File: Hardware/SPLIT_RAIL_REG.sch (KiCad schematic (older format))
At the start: 21 parts, among them Q1 PMOS, U1 TPS65130

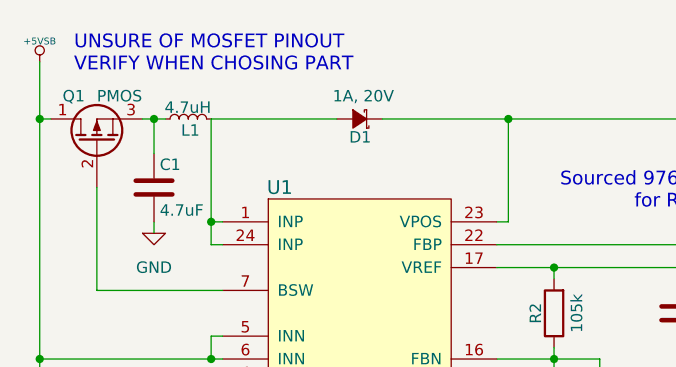
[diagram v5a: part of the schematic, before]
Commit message: Fixed schematic errors, added muse-v2-lib
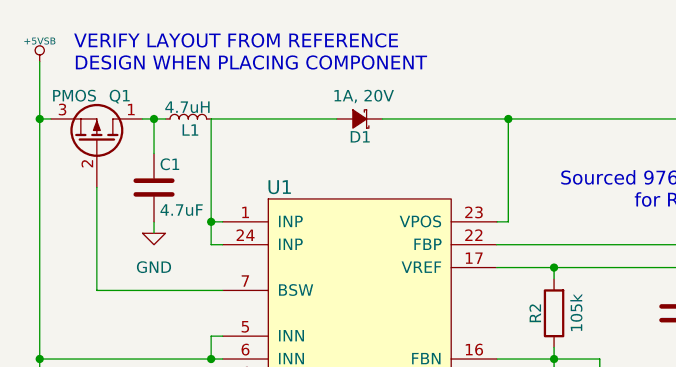
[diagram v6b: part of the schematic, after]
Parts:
- C1, C4, C5, C6, C7, C8, C9: footprint (none) -> Capacitors_SMD:C_0603
- C10, C3: footprint (none) -> Capacitors_SMD:C_1206
- C2: footprint (none) -> Capacitors_SMD:C_0402
- L1, L2: footprint (none) -> Choke_SMD:Choke_SMD_7.3x7.3_H3.5
- Q1: footprint (none) -> TO_SOT_Packages_SMD:SOT-23
- R1, R2, R3, R4, R5: footprint (none) -> Resistors_SMD:R_0402
- U1: footprint (none) -> MF_Switches:MF_Switches-TACT4.2MM
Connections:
- net +5VSB: now also Q1.3 (S); no longer Q1.1 (D)
- net at C1.1, L1.1: now also Q1.1 (D); no longer Q1.3 (S)
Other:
- note added: "VERIFY LAYOUT FROM REFERENCE\nDESIGN WHEN PLACING COMPONENT"
- note removed: "UNSURE OF MOSFET PINOUT\nVERIFY WHEN CHOSING PART"
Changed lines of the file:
@@
 F 0 "U1" H 5100 2950 60  0000 C CNN
 F 1 "TPS65130" H 5800 1150 60  0000 C CNN
-F 2 "" H 5050 2900 60  0001 C CNN
+F 2 "MF_Switches:MF_Switches-TACT4.2MM" H 5050 2900 60  0001 C CNN
 F 3 "" H 5050 2900 60  0001 C CNN
 	1    5050 2900
@@
 $EndComp
 $Comp
-L GND-RESCUE-museV2-RESCUE-museV2 #PWR01
+L GND-RESCUE-museV2-RESCUE-museV2 #PWR10
 U 1 1 57DAC9F2
 P 5450 5000
-F 0 "#PWR01" H 5450 4750 50  0001 C CNN
+F 0 "#PWR10" H 5450 4750 50  0001 C CNN
 F 1 "GND" H 5450 4850 50  0000 C CNN
 F 2 "" H 5450 5000 50  0000 C CNN
@@
 F 0 "C8" H 6125 4850 50  0000 L CNN
 F 1 "10nF" H 6125 4650 50  0000 L CNN
-F 2 "" H 6138 4600 50  0000 C CNN
+F 2 "Capacitors_SMD:C_0603" H 6138 4600 50  0001 C CNN
 F 3 "10 nF, ceramic, 16 V, X7R" H 6100 4750 50  0001 C CNN
 	1    6100 4750
@@
 F 0 "C9" H 6375 4850 50  0000 L CNN
 F 1 "4.7nF" H 6375 4650 50  0000 L CNN
-F 2 "" H 6388 4600 50  0000 C CNN
+F 2 "Capacitors_SMD:C_0603" H 6388 4600 50  0001 C CNN
 F 3 "4.7 nF, 50 V, C0G" H 6350 4750 50  0001 C CNN
 	1    6350 4750
@@
 $EndComp
 $Comp
-L GND-RESCUE-museV2-RESCUE-museV2 #PWR02
+L GND-RESCUE-museV2-RESCUE-museV2 #PWR11
 U 1 1 57DACA83
 P 6100 5000
-F 0 "#PWR02" H 6100 4750 50  0001 C CNN
+F 0 "#PWR11" H 6100 4750 50  0001 C CNN
 F 1 "GND" H 6100 4850 50  0000 C CNN
 F 2 "" H 6100 5000 50  0000 C CNN
@@
 $EndComp
 $Comp
-L GND-RESCUE-museV2-RESCUE-museV2 #PWR03
+L GND-RESCUE-museV2-RESCUE-museV2 #PWR12
 U 1 1 57DACA97
 P 6350 5000
-F 0 "#PWR03" H 6350 4750 50  0001 C CNN
+F 0 "#PWR12" H 6350 4750 50  0001 C CNN
 F 1 "GND" H 6350 4850 50  0000 C CNN
 F 2 "" H 6350 5000 50  0000 C CNN
@@
 F 0 "L2" H 6630 4790 50  0000 L CNN
 F 1 "4.7uH" H 6630 4710 50  0000 L CNN
-F 2 "" H 6600 4750 50  0000 C CNN
+F 2 "Choke_SMD:Choke_SMD_7.3x7.3_H3.5" H 6600 4750 50  0001 C CNN
 F 3 "Wurth Elektronik 7447789004" H 6600 4750 50  0001 C CNN
 	1    6600 4750
@@
 $EndComp
 $Comp
-L GND-RESCUE-museV2-RESCUE-museV2 #PWR04
+L GND-RESCUE-museV2-RESCUE-museV2 #PWR13
 U 1 1 57DACC08
 P 6600 5000
-F 0 "#PWR04" H 6600 4750 50  0001 C CNN
+F 0 "#PWR13" H 6600 4750 50  0001 C CNN
 F 1 "GND" H 6600 4850 50  0000 C CNN
 F 2 "" H 6600 5000 50  0000 C CNN
@@
 $EndComp
 $Comp
-L GND-RESCUE-museV2-RESCUE-museV2 #PWR05
+L GND-RESCUE-museV2-RESCUE-museV2 #PWR14
 U 1 1 57DACD4E
 P 7550 5000
-F 0 "#PWR05" H 7550 4750 50  0001 C CNN
+F 0 "#PWR14" H 7550 4750 50  0001 C CNN
 F 1 "GND" H 7550 4850 50  0000 C CNN
 F 2 "" H 7550 5000 50  0000 C CNN
@@
 F 0 "R4" V 6200 3800 50  0000 C CNN
 F 1 "1.3M" V 6300 3800 50  0000 C CNN
-F 2 "" V 6230 3800 50  0000 C CNN
+F 2 "Resistors_SMD:R_0402" V 6230 3800 50  0001 C CNN
 F 3 "" H 6300 3800 50  0000 C CNN
 	1    6300 3800
@@
 F 0 "C5" H 6525 3900 50  0000 L CNN
 F 1 "5.77pF" H 6525 3700 50  0000 L CNN
-F 2 "" H 6538 3650 50  0000 C CNN
+F 2 "Capacitors_SMD:C_0603" H 6538 3650 50  0001 C CNN
 F 3 "" H 6500 3800 50  0000 C CNN
 	1    6500 3800
@@
 F 0 "R2" V 6380 3400 50  0000 C CNN
 F 1 "105k" V 6200 3400 50  0000 C CNN
-F 2 "" V 6230 3400 50  0000 C CNN
+F 2 "Resistors_SMD:R_0402" V 6230 3400 50  0001 C CNN
 F 3 "" H 6300 3400 50  0000 C CNN
 	1    6300 3400
@@
 F 0 "C4" H 6875 3500 50  0000 L CNN
 F 1 "220nF" H 6875 3300 50  0000 L CNN
-F 2 "" H 6888 3250 50  0000 C CNN
+F 2 "Capacitors_SMD:C_0603" H 6888 3250 50  0001 C CNN
 F 3 "220 nF, ceramic, 6.3 V, X5R" H 6850 3400 50  0001 C CNN
 	1    6850 3400
@@
 Connection ~ 6300 3200
 $Comp
-L GND-RESCUE-museV2-RESCUE-museV2 #PWR06
+L GND-RESCUE-museV2-RESCUE-museV2 #PWR4
 U 1 1 57DADA89
 P 6850 3750
-F 0 "#PWR06" H 6850 3500 50  0001 C CNN
+F 0 "#PWR4" H 6850 3500 50  0001 C CNN
 F 1 "GND" H 6850 3600 50  0000 C CNN
 F 2 "" H 6850 3750 50  0000 C CNN
@@
 F 0 "C7" H 4575 4850 50  0000 L CNN
 F 1 "100nF" H 4575 4650 50  0000 L CNN
-F 2 "" H 4588 4600 50  0000 C CNN
+F 2 "Capacitors_SMD:C_0603" H 4588 4600 50  0001 C CNN
 F 3 "0.1 µF, ceramic, 10 V, X5R" H 4550 4750 50  0001 C CNN
 	1    4550 4750
@@
 F 0 "R5" V 4380 4500 50  0000 C CNN
 F 1 "100" V 4300 4500 50  0000 C CNN
-F 2 "" V 4230 4500 50  0000 C CNN
+F 2 "Resistors_SMD:R_0402" V 4230 4500 50  0001 C CNN
 F 3 "" H 4300 4500 50  0000 C CNN
 	1    4300 4500
@@
 	4050 4500 4150 4500
 $Comp
-L GND-RESCUE-museV2-RESCUE-museV2 #PWR07
+L GND-RESCUE-museV2-RESCUE-museV2 #PWR9
 U 1 1 57DAE30A
 P 4550 5000
-F 0 "#PWR07" H 4550 4750 50  0001 C CNN
+F 0 "#PWR9" H 4550 4750 50  0001 C CNN
 F 1 "GND" H 4550 4850 50  0000 C CNN
 F 2 "" H 4550 5000 50  0000 C CNN
@@
 	4550 5000 4550 4900
 $Comp
-L GND-RESCUE-museV2-RESCUE-museV2 #PWR08
+L GND-RESCUE-museV2-RESCUE-museV2 #PWR8
 U 1 1 57DAE3B0
 P 4050 5000
-F 0 "#PWR08" H 4050 4750 50  0001 C CNN
+F 0 "#PWR8" H 4050 4750 50  0001 C CNN
 F 1 "GND" H 4050 4850 50  0000 C CNN
 F 2 "" H 4050 5000 50  0000 C CNN
@@
 F 0 "Q1" V 4500 2800 50  0000 R CNN
 F 1 "PMOS" V 4500 2650 50  0000 R CNN
-F 2 "" H 4500 2750 50  0000 C CNN
+F 2 "TO_SOT_Packages_SMD:SOT-23" H 4500 2750 50  0001 C CNN
 F 3 "MOSFET, P-channel, 12 V, 4 A, Vishay" H 4300 2650 50  0001 C CNN
 	1    4300 2650
-	0    -1   -1   0
+	0    1    -1   0
 $EndComp
 Connection ~ 4050 2550
@@
 F 0 "C1" H 4575 2950 50  0000 L CNN
 F 1 "4.7uF" H 4575 2750 50  0000 L CNN
-F 2 "" H 4588 2700 50  0000 C CNN
+F 2 "Capacitors_SMD:C_0603" H 4588 2700 50  0001 C CNN
 F 3 "4.7 µF, ceramic, 6.3 V, X5R" H 4550 2850 50  0001 C CNN
 	1    4550 2850
@@
 $EndComp
 $Comp
-L GND-RESCUE-museV2-RESCUE-museV2 #PWR09
+L GND-RESCUE-museV2-RESCUE-museV2 #PWR3
 U 1 1 57DAEBCD
 P 4550 3050
-F 0 "#PWR09" H 4550 2800 50  0001 C CNN
+F 0 "#PWR3" H 4550 2800 50  0001 C CNN
 F 1 "GND" H 4550 2900 50  0000 C CNN
 F 2 "" H 4550 3050 50  0000 C CNN
@@
 F 0 "D1" H 5400 2630 50  0000 L CNN
 F 1 "1A, 20V" H 5300 2450 50  0000 L CNN
-F 2 "" V 5450 2550 50  0000 C CNN
+F 2 "" V 5450 2550 50  0001 C CNN
 F 3 "Schottky, 1 A, 20 V, Onsemi MBRM120" V 5450 2550 50  0001 C CNN
 	1    5450 2550
@@
 F 0 "R3" V 7330 3400 50  0000 C CNN
 F 1 "85.8k" V 7150 3400 50  0000 C CNN
-F 2 "" V 7180 3400 50  0000 C CNN
+F 2 "Resistors_SMD:R_0402" V 7180 3400 50  0001 C CNN
 F 3 "" H 7250 3400 50  0000 C CNN
 	1    7250 3400
@@
 $EndComp
 $Comp
-L GND-RESCUE-museV2-RESCUE-museV2 #PWR010
+L GND-RESCUE-museV2-RESCUE-museV2 #PWR5
 U 1 1 57DAF32E
 P 7250 3750
-F 0 "#PWR010" H 7250 3500 50  0001 C CNN
+F 0 "#PWR5" H 7250 3500 50  0001 C CNN
 F 1 "GND" H 7250 3600 50  0000 C CNN
 F 2 "" H 7250 3750 50  0000 C CNN
@@
 F 0 "R1" V 7130 2850 50  0000 C CNN
 F 1 "975k" V 7050 2850 50  0000 C CNN
-F 2 "" V 6980 2850 50  0000 C CNN
+F 2 "Resistors_SMD:R_0402" V 6980 2850 50  0001 C CNN
 F 3 "" H 7050 2850 50  0000 C CNN
 	1    7050 2850
@@
 F 0 "C2" H 7275 2950 50  0000 L CNN
 F 1 "6.97pF" H 7275 2750 50  0000 L CNN
-F 2 "" H 7288 2700 50  0000 C CNN
+F 2 "Capacitors_SMD:C_0402" H 7288 2700 50  0001 C CNN
 F 3 "" H 7250 2850 50  0000 C CNN
 	1    7250 2850
@@
 F 0 "C3" H 7575 2950 50  0000 L CNN
 F 1 "4.7uF" H 7575 2750 50  0000 L CNN
-F 2 "" H 7588 2700 50  0000 C CNN
+F 2 "Capacitors_SMD:C_1206" H 7588 2700 50  0001 C CNN
 F 3 "4 x 4.7 µF, ceramic, 25 V, X7R" H 7550 2850 50  0001 C CNN
 	1    7550 2850
@@
 Connection ~ 7550 2550
 $Comp
-L GND-RESCUE-museV2-RESCUE-museV2 #PWR011
+L GND-RESCUE-museV2-RESCUE-museV2 #PWR6
 U 1 1 57DAF96B
 P 7550 3750
-F 0 "#PWR011" H 7550 3500 50  0001 C CNN
+F 0 "#PWR6" H 7550 3500 50  0001 C CNN
 F 1 "GND" H 7550 3600 50  0000 C CNN
 F 2 "" H 7550 3750 50  0000 C CNN
@@
 F 0 "C6" H 4075 4850 50  0000 L CNN
 F 1 "4.7uF" H 4075 4650 50  0000 L CNN
-F 2 "" H 4088 4600 50  0000 C CNN
+F 2 "Capacitors_SMD:C_0603" H 4088 4600 50  0001 C CNN
 F 3 "4.7 µF, ceramic, 6.3 V, X5R" H 4050 4750 50  0001 C CNN
 	1    4050 4750
@@
 F 0 "C10" H 7575 4850 50  0000 L CNN
 F 1 "4.7uF" H 7575 4650 50  0000 L CNN
-F 2 "" H 7588 4600 50  0000 C CNN
+F 2 "Capacitors_SMD:C_1206" H 7588 4600 50  0001 C CNN
 F 3 "4 x 4.7 µF, ceramic, 25 V, X7R" H 7550 4750 50  0001 C CNN
 	1    7550 4750
@@
 F 0 "L1" V 4650 2500 50  0000 L CNN
 F 1 "4.7uH" V 4750 2450 50  0000 L CNN
-F 2 "" H 4700 2550 50  0000 C CNN
+F 2 "Choke_SMD:Choke_SMD_7.3x7.3_H3.5" H 4700 2550 50  0001 C CNN
 F 3 "Wurth Elektronik 7447789004" H 4700 2550 50  0001 C CNN
 	1    4700 2550
@@
 $EndComp
 Text Notes 4200 2350 0    60   ~ 0
-UNSURE OF MOSFET PINOUT\nVERIFY WHEN CHOSING PART
+VERIFY LAYOUT FROM REFERENCE\nDESIGN WHEN PLACING COMPONENT
 $Comp
 L D_Schottky_Small D2
@@
 F 0 "D2" H 7000 4280 50  0000 L CNN
 F 1 "1A, 20V" H 6900 4100 50  0000 L CNN
-F 2 "" V 7050 4200 50  0000 C CNN
+F 2 "" V 7050 4200 50  0001 C CNN
 F 3 "Schottky, 1 A, 20 V, Onsemi MBRM120" V 7050 4200 50  0001 C CNN
 	1    7050 4200
@@
 $EndComp
 $Comp
-L +5VSB #PWR012
+L +5VSB #PWR1
 U 1 1 57F87DFC
 P 4050 2300
-F 0 "#PWR012" H 4050 2390 20  0001 C CNN
+F 0 "#PWR1" H 4050 2390 20  0001 C CNN
 F 1 "+5VSB" H 4050 2390 30  0000 C CNN
 F 2 "" H 4050 2300 60  0000 C CNN
@@
 	7850 2550 7850 2300
 $Comp
-L +15VSB #PWR013
+L +15VSB #PWR2
 U 1 1 57F88166
 P 7850 2300
-F 0 "#PWR013" H 7850 2150 50  0001 C CNN
+F 0 "#PWR2" H 7850 2150 50  0001 C CNN
 F 1 "+15VSB" H 7850 2440 50  0000 C CNN
 F 2 "" H 7850 2300 50  0000 C CNN

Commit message: Added proper audio connectors to schematic
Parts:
- D1, D2: footprint (none) -> muse-v2-lib:DO-216-AA
- L1, L2: footprint Choke_SMD:Choke_SMD_7.3x7.3_H3.5 -> muse-v2-lib:7.3mm-Inductor
- U1: footprint MF_Switches:MF_Switches-TACT4.2MM -> Housings_DFN_QFN:QFN-24-1EP_4x4mm_Pitch0.5mm
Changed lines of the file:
@@
 F 0 "U1" H 5100 2950 60  0000 C CNN
 F 1 "TPS65130" H 5800 1150 60  0000 C CNN
-F 2 "MF_Switches:MF_Switches-TACT4.2MM" H 5050 2900 60  0001 C CNN
+F 2 "Housings_DFN_QFN:QFN-24-1EP_4x4mm_Pitch0.5mm" H 5050 2900 60  0001 C CNN
 F 3 "" H 5050 2900 60  0001 C CNN
 	1    5050 2900
@@
 $EndComp
 $Comp
-L GND-RESCUE-museV2-RESCUE-museV2 #PWR10
+L GND-RESCUE-museV2-RESCUE-museV2 #PWR01
 U 1 1 57DAC9F2
 P 5450 5000
-F 0 "#PWR10" H 5450 4750 50  0001 C CNN
+F 0 "#PWR01" H 5450 4750 50  0001 C CNN
 F 1 "GND" H 5450 4850 50  0000 C CNN
 F 2 "" H 5450 5000 50  0000 C CNN
@@
 $EndComp
 $Comp
-L GND-RESCUE-museV2-RESCUE-museV2 #PWR11
+L GND-RESCUE-museV2-RESCUE-museV2 #PWR02
 U 1 1 57DACA83
 P 6100 5000
-F 0 "#PWR11" H 6100 4750 50  0001 C CNN
+F 0 "#PWR02" H 6100 4750 50  0001 C CNN
 F 1 "GND" H 6100 4850 50  0000 C CNN
 F 2 "" H 6100 5000 50  0000 C CNN
@@
 $EndComp
 $Comp
-L GND-RESCUE-museV2-RESCUE-museV2 #PWR12
+L GND-RESCUE-museV2-RESCUE-museV2 #PWR03
 U 1 1 57DACA97
 P 6350 5000
-F 0 "#PWR12" H 6350 4750 50  0001 C CNN
+F 0 "#PWR03" H 6350 4750 50  0001 C CNN
 F 1 "GND" H 6350 4850 50  0000 C CNN
 F 2 "" H 6350 5000 50  0000 C CNN
@@
 F 0 "L2" H 6630 4790 50  0000 L CNN
 F 1 "4.7uH" H 6630 4710 50  0000 L CNN
-F 2 "Choke_SMD:Choke_SMD_7.3x7.3_H3.5" H 6600 4750 50  0001 C CNN
+F 2 "muse-v2-lib:7.3mm-Inductor" H 6600 4750 50  0001 C CNN
 F 3 "Wurth Elektronik 7447789004" H 6600 4750 50  0001 C CNN
 	1    6600 4750
@@
 $EndComp
 $Comp
-L GND-RESCUE-museV2-RESCUE-museV2 #PWR13
+L GND-RESCUE-museV2-RESCUE-museV2 #PWR04
 U 1 1 57DACC08
 P 6600 5000
-F 0 "#PWR13" H 6600 4750 50  0001 C CNN
+F 0 "#PWR04" H 6600 4750 50  0001 C CNN
 F 1 "GND" H 6600 4850 50  0000 C CNN
 F 2 "" H 6600 5000 50  0000 C CNN
@@
 $EndComp
 $Comp
-L GND-RESCUE-museV2-RESCUE-museV2 #PWR14
+L GND-RESCUE-museV2-RESCUE-museV2 #PWR05
 U 1 1 57DACD4E
 P 7550 5000
-F 0 "#PWR14" H 7550 4750 50  0001 C CNN
+F 0 "#PWR05" H 7550 4750 50  0001 C CNN
 F 1 "GND" H 7550 4850 50  0000 C CNN
 F 2 "" H 7550 5000 50  0000 C CNN
@@
 Connection ~ 6300 3200
 $Comp
-L GND-RESCUE-museV2-RESCUE-museV2 #PWR4
+L GND-RESCUE-museV2-RESCUE-museV2 #PWR06
 U 1 1 57DADA89
 P 6850 3750
-F 0 "#PWR4" H 6850 3500 50  0001 C CNN
+F 0 "#PWR06" H 6850 3500 50  0001 C CNN
 F 1 "GND" H 6850 3600 50  0000 C CNN
 F 2 "" H 6850 3750 50  0000 C CNN
@@
 	4050 4500 4150 4500
 $Comp
-L GND-RESCUE-museV2-RESCUE-museV2 #PWR9
+L GND-RESCUE-museV2-RESCUE-museV2 #PWR07
 U 1 1 57DAE30A
 P 4550 5000
-F 0 "#PWR9" H 4550 4750 50  0001 C CNN
+F 0 "#PWR07" H 4550 4750 50  0001 C CNN
 F 1 "GND" H 4550 4850 50  0000 C CNN
 F 2 "" H 4550 5000 50  0000 C CNN
@@
 	4550 5000 4550 4900
 $Comp
-L GND-RESCUE-museV2-RESCUE-museV2 #PWR8
+L GND-RESCUE-museV2-RESCUE-museV2 #PWR08
 U 1 1 57DAE3B0
 P 4050 5000
-F 0 "#PWR8" H 4050 4750 50  0001 C CNN
+F 0 "#PWR08" H 4050 4750 50  0001 C CNN
 F 1 "GND" H 4050 4850 50  0000 C CNN
 F 2 "" H 4050 5000 50  0000 C CNN
@@
 $EndComp
 $Comp
-L GND-RESCUE-museV2-RESCUE-museV2 #PWR3
+L GND-RESCUE-museV2-RESCUE-museV2 #PWR09
 U 1 1 57DAEBCD
 P 4550 3050
-F 0 "#PWR3" H 4550 2800 50  0001 C CNN
+F 0 "#PWR09" H 4550 2800 50  0001 C CNN
 F 1 "GND" H 4550 2900 50  0000 C CNN
 F 2 "" H 4550 3050 50  0000 C CNN
@@
 F 0 "D1" H 5400 2630 50  0000 L CNN
 F 1 "1A, 20V" H 5300 2450 50  0000 L CNN
-F 2 "" V 5450 2550 50  0001 C CNN
+F 2 "muse-v2-lib:DO-216-AA" V 5450 2550 50  0001 C CNN
 F 3 "Schottky, 1 A, 20 V, Onsemi MBRM120" V 5450 2550 50  0001 C CNN
 	1    5450 2550
@@
 $EndComp
 $Comp
-L GND-RESCUE-museV2-RESCUE-museV2 #PWR5
+L GND-RESCUE-museV2-RESCUE-museV2 #PWR010
 U 1 1 57DAF32E
 P 7250 3750
-F 0 "#PWR5" H 7250 3500 50  0001 C CNN
+F 0 "#PWR010" H 7250 3500 50  0001 C CNN
 F 1 "GND" H 7250 3600 50  0000 C CNN
 F 2 "" H 7250 3750 50  0000 C CNN
@@
 Connection ~ 7550 2550
 $Comp
-L GND-RESCUE-museV2-RESCUE-museV2 #PWR6
+L GND-RESCUE-museV2-RESCUE-museV2 #PWR011
 U 1 1 57DAF96B
 P 7550 3750
-F 0 "#PWR6" H 7550 3500 50  0001 C CNN
+F 0 "#PWR011" H 7550 3500 50  0001 C CNN
 F 1 "GND" H 7550 3600 50  0000 C CNN
 F 2 "" H 7550 3750 50  0000 C CNN
@@
 F 0 "L1" V 4650 2500 50  0000 L CNN
 F 1 "4.7uH" V 4750 2450 50  0000 L CNN
-F 2 "Choke_SMD:Choke_SMD_7.3x7.3_H3.5" H 4700 2550 50  0001 C CNN
+F 2 "muse-v2-lib:7.3mm-Inductor" H 4700 2550 50  0001 C CNN
 F 3 "Wurth Elektronik 7447789004" H 4700 2550 50  0001 C CNN
 	1    4700 2550
@@
 F 0 "D2" H 7000 4280 50  0000 L CNN
 F 1 "1A, 20V" H 6900 4100 50  0000 L CNN
-F 2 "" V 7050 4200 50  0001 C CNN
+F 2 "muse-v2-lib:DO-216-AA" V 7050 4200 50  0001 C CNN
 F 3 "Schottky, 1 A, 20 V, Onsemi MBRM120" V 7050 4200 50  0001 C CNN
 	1    7050 4200
@@
 $EndComp
 $Comp
-L +5VSB #PWR1
+L +5VSB #PWR012
 U 1 1 57F87DFC
 P 4050 2300
-F 0 "#PWR1" H 4050 2390 20  0001 C CNN
+F 0 "#PWR012" H 4050 2390 20  0001 C CNN
 F 1 "+5VSB" H 4050 2390 30  0000 C CNN
 F 2 "" H 4050 2300 60  0000 C CNN
@@
 	7850 2550 7850 2300
 $Comp
-L +15VSB #PWR2
+L +15VSB #PWR013
 U 1 1 57F88166
 P 7850 2300
-F 0 "#PWR2" H 7850 2150 50  0001 C CNN
+F 0 "#PWR013" H 7850 2150 50  0001 C CNN
 F 1 "+15VSB" H 7850 2440 50  0000 C CNN
 F 2 "" H 7850 2300 50  0000 C CNN

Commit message: Routing split rail DC/DC converter
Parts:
- U1: footprint Housings_DFN_QFN:QFN-24-1EP_4x4mm_Pitch0.5mm -> muse-v2-lib:QFN-24-1EP_4x4mm_Pitch0.5mm_THERMAL
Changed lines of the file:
@@
 F 0 "U1" H 5100 2950 60  0000 C CNN
 F 1 "TPS65130" H 5800 1150 60  0000 C CNN
-F 2 "Housings_DFN_QFN:QFN-24-1EP_4x4mm_Pitch0.5mm" H 5050 2900 60  0001 C CNN
+F 2 "muse-v2-lib:QFN-24-1EP_4x4mm_Pitch0.5mm_THERMAL" H 5050 2900 60  0001 C CNN
 F 3 "" H 5050 2900 60  0001 C CNN
 	1    5050 2900
